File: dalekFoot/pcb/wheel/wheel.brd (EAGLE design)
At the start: 100 x 100 mm, 75 parts, among them IC1 LM1117MP-3.3, IC3 LM1117MP-3.3, IC4 4051D, IC5 4051D, IC6 LM1117MP-3.3, U1 TB6612FNG(O,C,8,EL, U2 SS8050-SOT-23, U3 SS8050-SOT-23, U4 SS8050-SOT-23, U5 TB6612FNG(O,C,8,EL, U6 TB6612FNG(O,C,8,EL

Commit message: optimize routing
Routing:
- net BIN2.1: track 68.8 -> 59.2 mm, vias 4 -> 1
- net AIN2.1: track 55.1 -> 59.9 mm, vias 3 -> 4
- net AIN2.2: track 59.8 -> 63.3 mm
- net USART_TX: track 104.0 -> 105.6 mm
- net PWM3.A: track 32.1 -> 30.7 mm
- net BIN2.2: track 59.7 -> 60.9 mm
- net AIN3.1: track 25.7 -> 26.7 mm
- net VCC-DIGITAL: track 333.2 -> 334.1 mm
- net BUZZER: track 33.8 -> 34.7 mm
- net DIN3: track 70.4 -> 71.3 mm
- net PWM1.A: track 46.2 -> 47.0 mm
- net DIN4: track 66.5 -> 67.2 mm
- net I2C2_SCL: track 64.4 -> 65.0 mm
- net BIN1.2: track 65.0 -> 65.5 mm
- net SPI_MOSI: track 86.4 -> 86.7 mm, vias 2 -> 3
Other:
- outline, holes or cut-outs redrawn

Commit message: add logo
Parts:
- added U$3: COOBOC-PLACE, hqc-logo:COOBOC-PLACE
- added U$4: ASTRONANT, hqc-logo:ASTRONANT
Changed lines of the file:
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@@
 <attribute name="VALUE" x="83.34375" y="48.10125" size="1.27" layer="27" rot="R90"/>
 </element>
+<element name="U$3" library="hqc-logo" package="COOBOC-PLACE" value="COOBOC-PLACE" x="45.085" y="48.41875" rot="MR0"/>
+<element name="U$4" library="hqc-logo" package="ASTRONANT" value="ASTRONANT" x="57.15" y="50.32375" rot="MR0"/>
 </elements>
 <signals>

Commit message: move logo position
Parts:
- moved U$3 54.5 mm to (8.73, 7.78)
- moved U$4 54.4 mm to (21.6, 9.21)
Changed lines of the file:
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@@
 <grid distance="6.25" unitdist="mil" unit="mil" style="lines" multiple="1" display="yes" altdistance="0.025" altunitdist="inch" altunit="mil"/>
 <layers>
-<layer number="1" name="Top" color="4" fill="1" visible="yes" active="yes"/>
+<layer number="1" name="Top" color="4" fill="1" visible="no" active="yes"/>
 <layer number="2" name="Route2" color="1" fill="3" visible="no" active="no"/>
 <layer number="3" name="Route3" color="4" fill="3" visible="no" active="no"/>
@@
 <layer number="14" name="Route14" color="1" fill="6" visible="no" active="no"/>
 <layer number="15" name="Route15" color="4" fill="6" visible="no" active="no"/>
-<layer number="16" name="Bottom" color="1" fill="1" visible="yes" active="yes"/>
-<layer number="17" name="Pads" color="2" fill="1" visible="yes" active="yes"/>
+<layer number="16" name="Bottom" color="1" fill="1" visible="no" active="yes"/>
+<layer number="17" name="Pads" color="2" fill="1" visible="no" active="yes"/>
 <layer number="18" name="Vias" color="2" fill="1" visible="yes" active="yes"/>
 <layer number="19" name="Unrouted" color="6" fill="1" visible="yes" active="yes"/>
 <layer number="20" name="Dimension" color="15" fill="1" visible="yes" active="yes"/>
-<layer number="21" name="tPlace" color="7" fill="1" visible="yes" active="yes"/>
+<layer number="21" name="tPlace" color="7" fill="1" visible="no" active="yes"/>
 <layer number="22" name="bPlace" color="7" fill="1" visible="yes" active="yes"/>
-<layer number="23" name="tOrigins" color="15" fill="1" visible="yes" active="yes"/>
+<layer number="23" name="tOrigins" color="15" fill="1" visible="no" active="yes"/>
 <layer number="24" name="bOrigins" color="15" fill="1" visible="yes" active="yes"/>
-<layer number="25" name="tNames" color="7" fill="1" visible="yes" active="yes"/>
+<layer number="25" name="tNames" color="7" fill="1" visible="no" active="yes"/>
 <layer number="26" name="bNames" color="7" fill="1" visible="yes" active="yes"/>
-<layer number="27" name="tValues" color="7" fill="1" visible="yes" active="yes"/>
+<layer number="27" name="tValues" color="7" fill="1" visible="no" active="yes"/>
 <layer number="28" name="bValues" color="7" fill="1" visible="yes" active="yes"/>
-<layer number="29" name="tStop" color="7" fill="3" visible="yes" active="yes"/>
+<layer number="29" name="tStop" color="7" fill="3" visible="no" active="yes"/>
 <layer number="30" name="bStop" color="7" fill="6" visible="yes" active="yes"/>
-<layer number="31" name="tCream" color="7" fill="4" visible="yes" active="yes"/>
-<layer number="32" name="bCream" color="7" fill="5" visible="yes" active="yes"/>
-<layer number="33" name="tFinish" color="6" fill="3" visible="yes" active="yes"/>
-<layer number="34" name="bFinish" color="6" fill="6" visible="yes" active="yes"/>
-<layer number="35" name="tGlue" color="7" fill="4" visible="yes" active="yes"/>
-<layer number="36" name="bGlue" color="7" fill="5" visible="yes" active="yes"/>
-<layer number="37" name="tTest" color="7" fill="1" visible="yes" active="yes"/>
-<layer number="38" name="bTest" color="7" fill="1" visible="yes" active="yes"/>
-<layer number="39" name="tKeepout" color="4" fill="11" visible="yes" active="yes"/>
-<layer number="40" name="bKeepout" color="1" fill="11" visible="yes" active="yes"/>
-<layer number="41" name="tRestrict" color="4" fill="10" visible="yes" active="yes"/>
-<layer number="42" name="bRestrict" color="1" fill="10" visible="yes" active="yes"/>
-<layer number="43" name="vRestrict" color="2" fill="10" visible="yes" active="yes"/>
-<layer number="44" name="Drills" color="7" fill="1" visible="yes" active="yes"/>
-<layer number="45" name="Holes" color="7" fill="1" visible="yes" active="yes"/>
-<layer number="46" name="Milling" color="3" fill="1" visible="yes" active="yes"/>
-<layer number="47" name="Measures" color="7" fill="1" visible="yes" active="yes"/>
-<layer number="48" name="Document" color="7" fill="1" visible="yes" active="yes"/>
-<layer number="49" name="Reference" color="7" fill="1" visible="yes" active="yes"/>
+<layer number="31" name="tCream" color="7" fill="4" visible="no" active="yes"/>
+<layer number="32" name="bCream" color="7" fill="5" visible="no" active="yes"/>
+<layer number="33" name="tFinish" color="6" fill="3" visible="no" active="yes"/>
+<layer number="34" name="bFinish" color="6" fill="6" visible="no" active="yes"/>
+<layer number="35" name="tGlue" color="7" fill="4" visible="no" active="yes"/>
+<layer number="36" name="bGlue" color="7" fill="5" visible="no" active="yes"/>
+<layer number="37" name="tTest" color="7" fill="1" visible="no" active="yes"/>
+<layer number="38" name="bTest" color="7" fill="1" visible="no" active="yes"/>
+<layer number="39" name="tKeepout" color="4" fill="11" visible="no" active="yes"/>
+<layer number="40" name="bKeepout" color="1" fill="11" visible="no" active="yes"/>
+<layer number="41" name="tRestrict" color="4" fill="10" visible="no" active="yes"/>
+<layer number="42" name="bRestrict" color="1" fill="10" visible="no" active="yes"/>
+<layer number="43" name="vRestrict" color="2" fill="10" visible="no" active="yes"/>
+<layer number="44" name="Drills" color="7" fill="1" visible="no" active="yes"/>
+<layer number="45" name="Holes" color="7" fill="1" visible="no" active="yes"/>
+<layer number="46" name="Milling" color="3" fill="1" visible="no" active="yes"/>
+<layer number="47" name="Measures" color="7" fill="1" visible="no" active="yes"/>
+<layer number="48" name="Document" color="7" fill="1" visible="no" active="yes"/>
+<layer number="49" name="Reference" color="7" fill="1" visible="no" active="yes"/>
 <layer number="50" name="dxf" color="7" fill="1" visible="no" active="no"/>
-<layer number="51" name="tDocu" color="7" fill="1" visible="yes" active="yes"/>
-<layer number="52" name="bDocu" color="7" fill="1" visible="yes" active="yes"/>
+<layer number="51" name="tDocu" color="7" fill="1" visible="no" active="yes"/>
+<layer number="52" name="bDocu" color="7" fill="1" visible="no" active="yes"/>
 <layer number="56" name="wert" color="7" fill="1" visible="no" active="no"/>
 <layer number="90" name="Modules" color="5" fill="1" visible="no" active="no"/>
@@
 <layer number="98" name="Guide" color="6" fill="1" visible="no" active="no"/>
 <layer number="99" name="SpiceOrder" color="5" fill="1" visible="no" active="no"/>
-<layer number="100" name="Mark" color="13" fill="1" visible="yes" active="yes"/>
+<layer number="100" name="Mark" color="13" fill="1" visible="no" active="yes"/>
 <layer number="200" name="200bmp" color="1" fill="10" visible="no" active="no"/>
-<layer number="201" name="201bmp" color="2" fill="10" visible="yes" active="yes"/>
+<layer number="201" name="201bmp" color="2" fill="10" visible="no" active="yes"/>
 </layers>
 <board>
@@
 <attribute name="VALUE" x="83.34375" y="48.10125" size="1.27" layer="27" rot="R90"/>
 </element>
-<element name="U$3" library="hqc-logo" package="COOBOC-PLACE" value="COOBOC-PLACE" x="45.085" y="48.41875" rot="MR0"/>
-<element name="U$4" library="hqc-logo" package="ASTRONANT" value="ASTRONANT" x="57.15" y="50.32375" rot="MR0"/>
+<element name="U$3" library="hqc-logo" package="COOBOC-PLACE" value="COOBOC-PLACE" x="8.73125" y="7.77875" rot="MR0"/>
+<element name="U$4" library="hqc-logo" package="ASTRONANT" value="ASTRONANT" x="21.59" y="9.2075" rot="MR0"/>
 </elements>
 <signals>

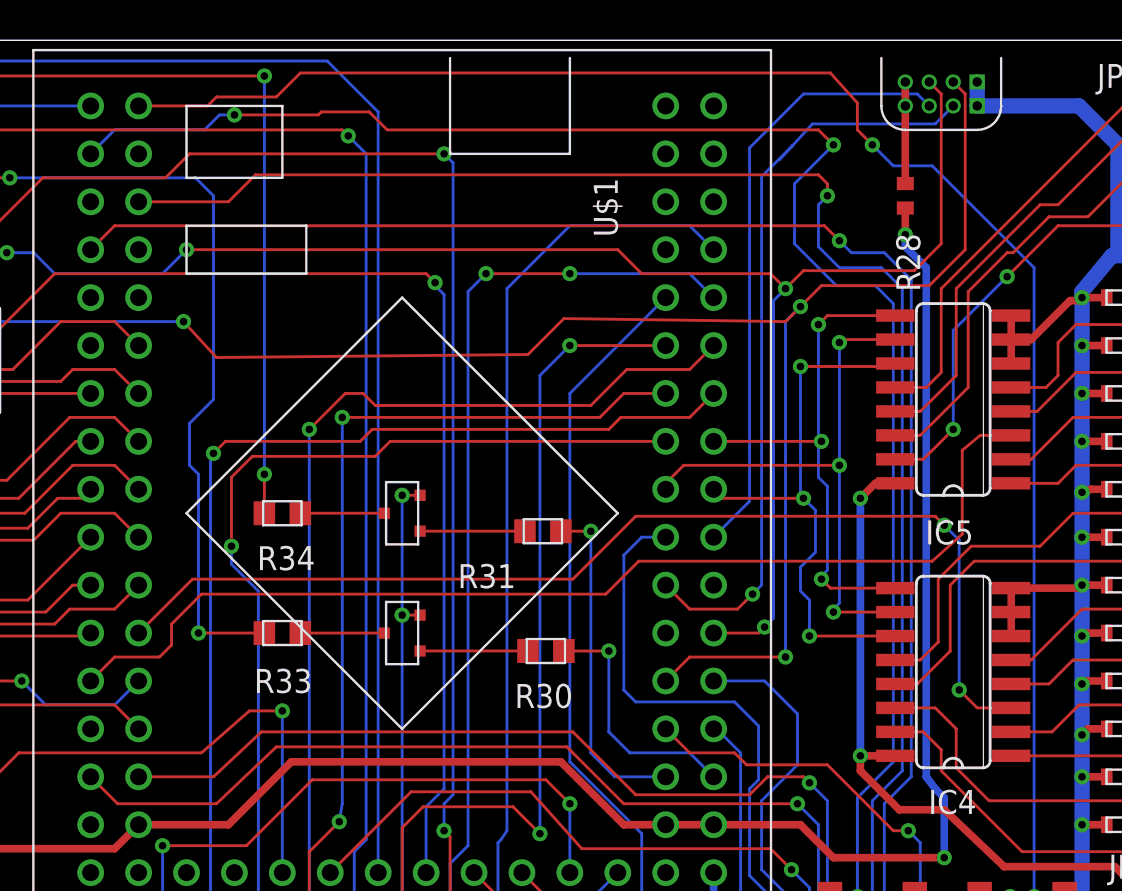
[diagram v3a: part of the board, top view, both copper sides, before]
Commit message: bugfix: clearance too small on debug port
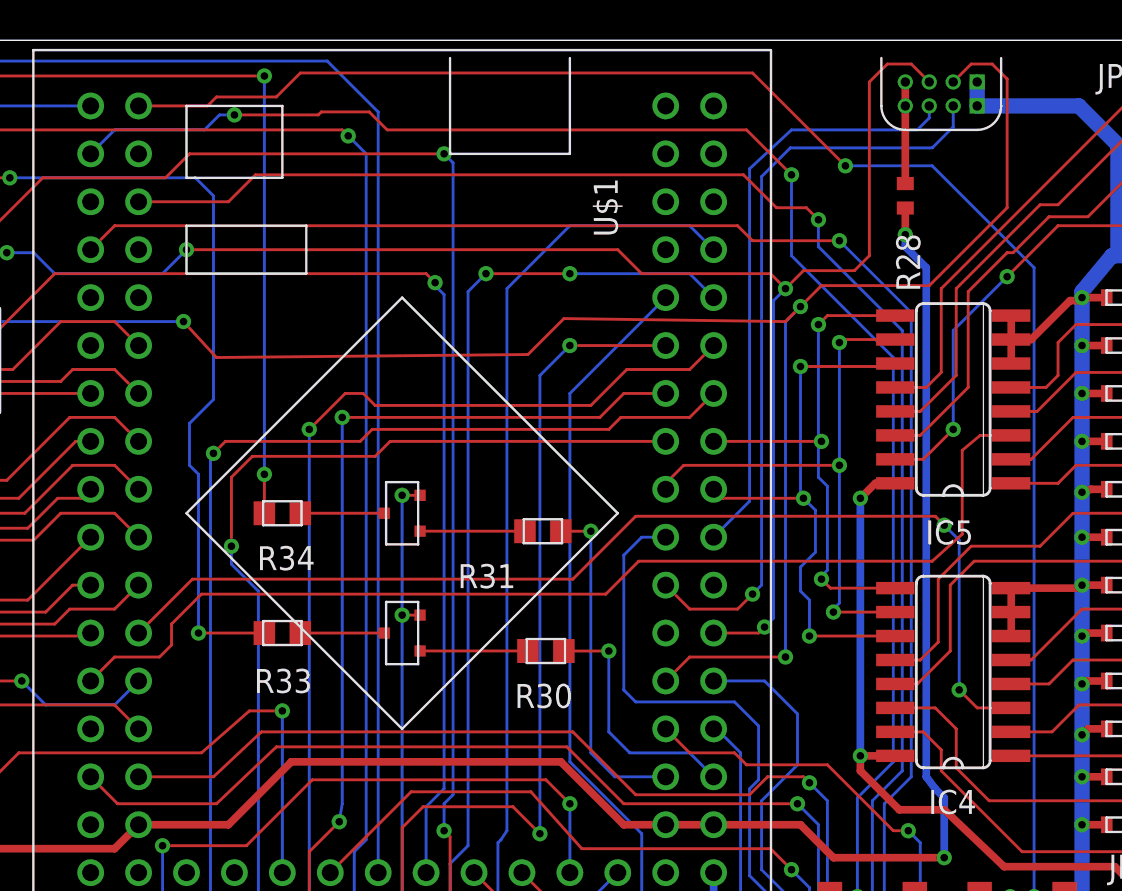
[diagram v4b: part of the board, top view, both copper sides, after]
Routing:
- net BUT3: track 96.7 -> 91.6 mm
- net USART_TX: track 105.6 -> 110.0 mm
- net DIN1: track 103.3 -> 100.2 mm
- net DIN2: track 100.5 -> 99.5 mm
- net BUT2: track 96.9 -> 96.0 mm
- net SWCLK: track 32.4 -> 31.5 mm

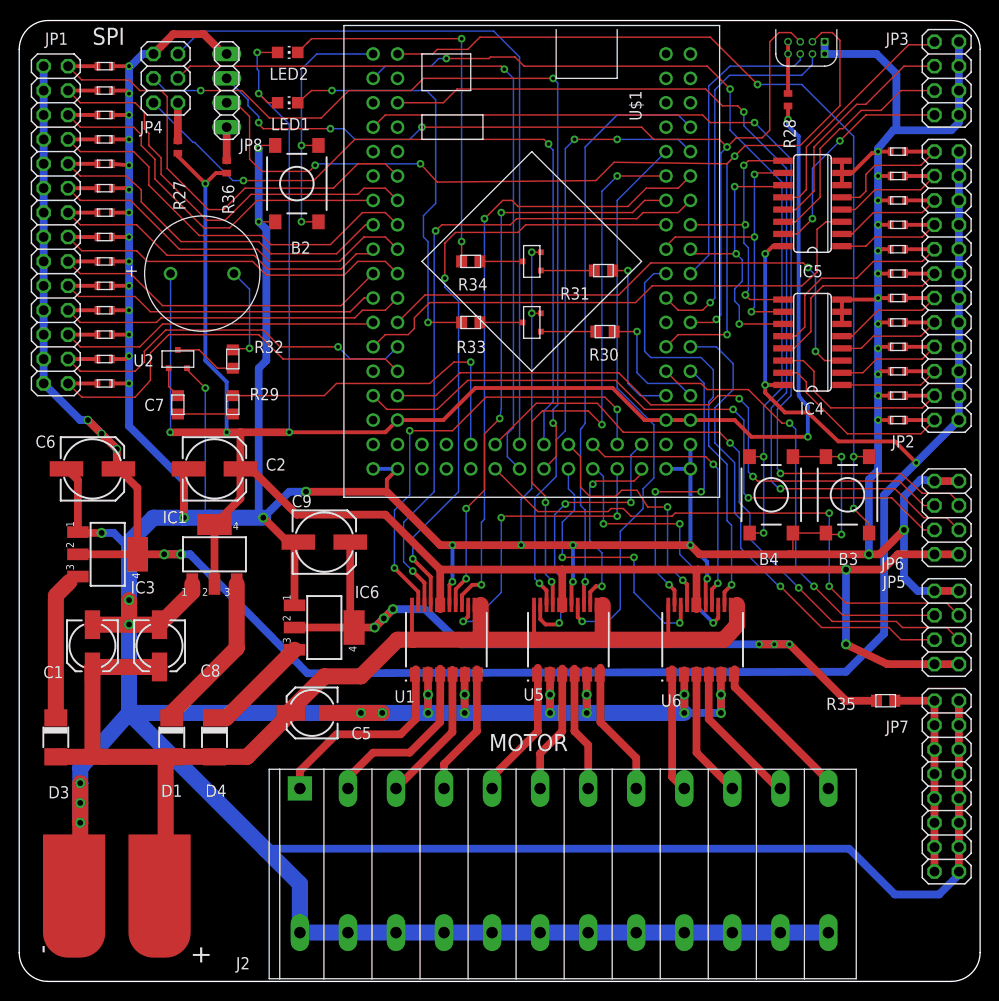
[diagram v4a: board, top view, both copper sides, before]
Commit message: Multiple bug fixed
1. add mouting holes
2. remove capacitor for buzzer
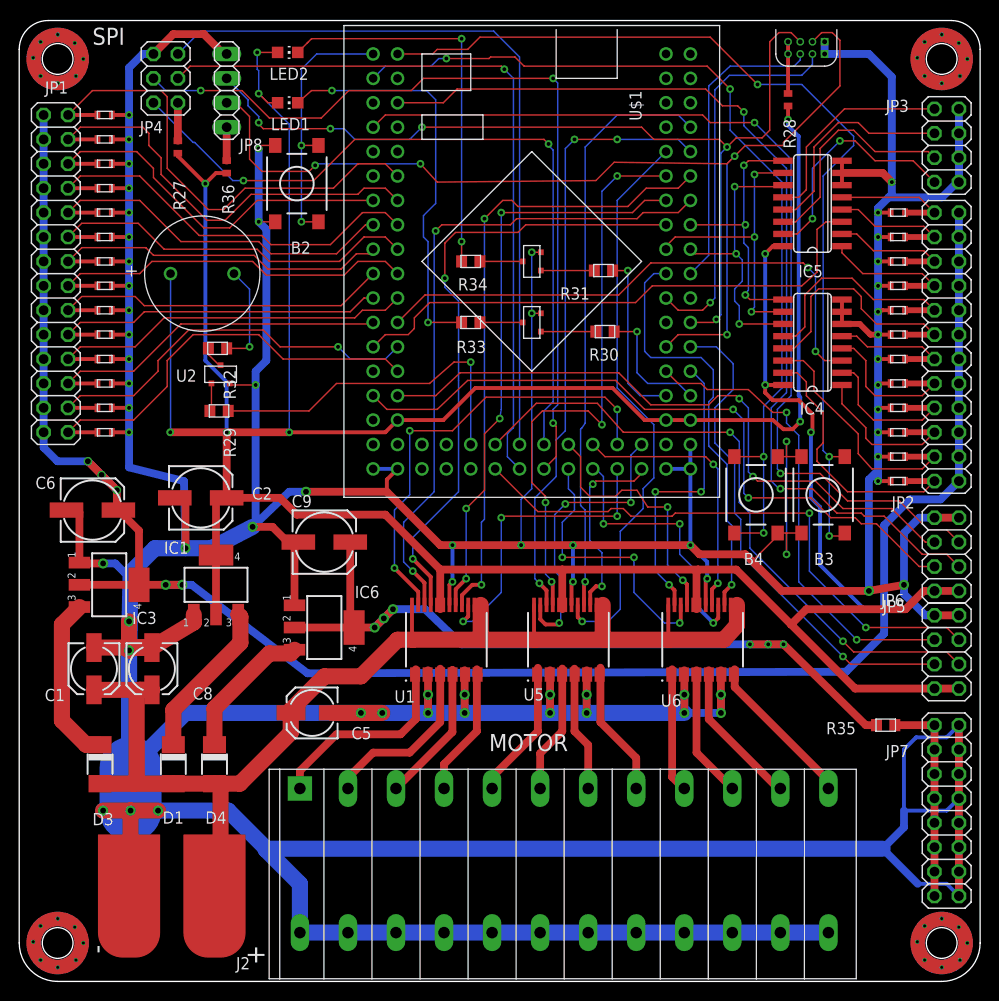
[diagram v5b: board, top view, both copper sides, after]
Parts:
- removed C7: (no value), hqc:0805
- added U$5, U$6, U$7, U$8: M3-MOUNTING-HOLE, hqc:M3-MOUNTING-HOLE
- moved U$4 62.0 mm to (83.5, 13.2)
- moved U$3 30.0 mm to (38.4, 11.9)
- moved JP3 6.98 mm to (96.5, 87.0)
- moved R18 6.35 mm to (91.4, 59.7)
- moved R20 6.35 mm to (91.4, 64.8)
- moved R22 6.35 mm to (91.4, 69.8)
- moved R15 6.35 mm to (91.4, 52.1)
- moved R16 6.35 mm to (91.4, 54.6)
- moved R17 6.35 mm to (91.4, 57.1)
- moved R19 6.35 mm to (91.4, 62.2)
- moved JP2 6.35 mm to (96.5, 66.0)
- moved R21 6.35 mm to (91.4, 67.3)
- moved R23 6.35 mm to (91.4, 72.4)
- moved R24 6.35 mm to (91.4, 74.9)
- moved R25 6.35 mm to (91.4, 77.5)
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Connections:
- removed net N$9: C7.P$1, R29.P$2
- net N$12: now also R29.P$2; no longer C7.P$2
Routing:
- net DGND: track 828.3 -> 867.5 mm, vias 65 -> 66
- net IR14: track 22.7 -> 29.1 mm
- net N$9: track 5.71 -> 0.00 mm
- net VCC-DIGITAL: track 334.1 -> 339.8 mm, vias 10 -> 8
- net BAT+: track 128.4 -> 123.5 mm
- net VCC-IR: track 242.9 -> 247.7 mm
- net IR16: track 13.3 -> 17.6 mm
- net N$15: track 6.50 -> 2.37 mm
- net IR15: track 22.6 -> 26.5 mm
- net N$2: track 11.3 -> 14.6 mm
- net BUT3: track 91.6 -> 94.8 mm
- net IR17: track 13.8 -> 16.9 mm
- net IR18: track 13.8 -> 16.8 mm
- net BUT2: track 96.0 -> 99.0 mm
- net AIN0: track 25.1 -> 22.2 mm
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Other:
- outline, holes or cut-outs redrawn

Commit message: Multiple changes
1. solve exti conflit of encoder port
2. optimize top route
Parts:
- moved R29 6.83 mm to (27.3, 61.4), turned to 270 degrees
- moved R32 5.15 mm to (17.8, 61.6), turned to 90 degrees
- moved R30 2.66 mm to (58.4, 68.4), turned to 270 degrees
- moved R31 2.56 mm to (58.4, 74.9), turned to 270 degrees
- moved R33 2.56 mm to (49.5, 68.3), turned to 270 degrees
- moved R34 2.54 mm to (49.5, 74.9), turned to 90 degrees
- moved U2 1.77 mm to (21.7, 61.6), turned to 90 degrees
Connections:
- removed net BUT4: U$1.P$60
- removed net BUT5: U$1.P$61
- net BUT1: now also U$1.P$61; no longer U$1.P$57
- net BUT2: now also U$1.P$62; no longer U$1.P$58
- net BUT3: now also U$1.P$63; no longer U$1.P$59
- net DIN1: now also U$1.P$57; no longer U$1.P$62
- net DIN2: now also U$1.P$58; no longer U$1.P$63
- net DIN3: now also U$1.P$59; no longer U$1.P$85
- net DIN4: now also U$1.P$60; no longer U$1.P$86
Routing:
- net DIN3: track 72.9 -> 99.9 mm, vias 2 -> 3
- net DIN4: track 68.8 -> 95.5 mm, vias 2 -> 3
- net BUZZER: track 35.8 -> 26.0 mm
- net BUT1: track 27.5 -> 19.0 mm
- net DIN1: track 101.7 -> 109.0 mm
- net IR10: track 52.8 -> 45.9 mm
- net N$18: track 10.7 -> 17.0 mm
- net AIN2.1: track 59.9 -> 54.3 mm
- net BUT3: track 94.8 -> 89.4 mm, vias 4 -> 3
- net LED2: track 17.8 -> 23.1 mm
- net AIN1.1: track 64.8 -> 59.9 mm
- net IR14: track 29.1 -> 24.7 mm
- net LED1: track 13.2 -> 17.4 mm
- net N$20: track 42.6 -> 46.2 mm
- net USART_TX: track 109.0 -> 106.2 mm
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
